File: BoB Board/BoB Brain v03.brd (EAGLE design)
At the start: 50 x 50 mm, 35 parts, among them Q1 MOSFET-NCHANNELAO3404A, Q9 MOSFET-NCHANNELAO3404A, U1 ATMEGA328P_TQFP, U3 +12v, U4 V_REG_317SMD, Y1 16MHZ

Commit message: Working on BoB board
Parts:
- removed JP2, JP3, JP4: (no value), SparkFun-Connectors:1X12
- added J1, J2, J4: (no value), SparkFun-Connectors:1X18
- moved Q9 58.0 mm to (1.80, 18.4)
- moved R17 58.0 mm to (10.9, 30.1)
- moved R19 58.0 mm to (5.90, 13.9)
- moved U4 58.0 mm to (10.1, 24.6)
- moved C10 58.0 mm to (10.8, 18.0)
- moved C11 58.0 mm to (15.0, 29.8)
- moved Q1 58.0 mm to (5.70, 18.1)
- moved R18 58.0 mm to (7.50, 32.7)
- moved R20 58.0 mm to (9.20, 14.9)
- moved R21 58.0 mm to (2.00, 21.3)
- moved R22 58.0 mm to (3.20, 23.4)
- moved U$1 56.5 mm to (18.7, 34.6), flipped to the bottom, turned to 270 degrees
- moved R11 53.1 mm to (23.1, 5.80)
- moved R12 53.0 mm to (26.6, 5.80)
- moved R13 53.0 mm to (24.9, 5.80)
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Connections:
- net N$5 renamed ATMEGA-RESET
- removed net 10: U1.14
- removed net 11: U1.15
- removed net 5: U1.9
- removed net 9: U1.13
- removed net N$10: JP4.11
- removed net N$16: JP4.10
- removed net N$17: JP4.9
- removed net N$18: JP4.8
- removed net N$19: JP4.7
- removed net N$20: JP4.6
- removed net N$21: JP4.5
- removed net N$22: JP4.4
- removed net N$23: JP4.3
- removed net N$24: JP4.2
- removed net N$25: JP4.1
- removed net N$3: U1.16
- removed net N$4: C5.2, R14.1, R2.2, S1.3, S1.4, U1.29
- removed net N$7: JP4.12
- new net 10~: J2.2, U1.14
- new net 11~: J2.1, U1.15
- new net 12: J2.6, U1.16
- new net 3~: J2.11, U1.1
- new net 4: J2.10, U1.2
- new net 5~: J2.9, U1.9
- new net 6~: J2.4, U1.10
- new net 7: J2.8, U1.11
- new net 8: J2.7, U1.12
- new net 9~: J2.3, U1.13
- new net A0: J2.18, U1.23
- new net A3: J2.15, U1.26
- new net A4-SDA: J2.14, U1.27
- new net A5-SCL: J2.13, U1.28
- new net ADC6: J2.12, U1.19
- new net ADC7: U1.22
- net 13: now also J2.5
- net 6V: now also J4.10, J4.11, J4.12, J4.13, J4.14, J4.15, J4.16, J4.17, J4.18, J4.5, J4.6, J4.7, J4.8, J4.9; no longer JP3.10, JP3.11, JP3.12, JP3.9
- net A1: now also J2.17
- net A2: now also J2.16
- net GND: now also J1.1, J1.10, J1.11, J1.12, J1.13, J1.14, J1.15, J1.16, J1.17, J1.18, J1.2, J1.3, J1.4, J1.5, J1.6, J1.7, J1.8, J1.9; no longer JP2.1, JP2.10, JP2.11, JP2.12, JP2.2, JP2.3, JP2.4, JP2.5, JP2.6, JP2.7, JP2.8, JP2.9
- net PIN_PWR: now also J4.1, J4.2, J4.3, J4.4; no longer JP3.1, JP3.2, JP3.3, JP3.4, JP3.5, JP3.6, JP3.7, JP3.8
- net RESET: now also C5.2, R14.1, R2.2, S1.3, S1.4, U1.29
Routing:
- net PIN_PWR: track 85.4 -> 0.00 mm
- net VCC: track 68.8 -> 43.1 mm
- net 6V: track 15.8 -> 0.00 mm
- net RAW: track 80.7 -> 68.7 mm
- net N$4: track 11.3 -> 0.00 mm
- net RESET: track 0.00 -> 11.2 mm
- net N$2: track 4.08 -> 0.00 mm
- net N$1: track 3.26 -> 0.00 mm
- net N$11: track 2.01 -> 0.00 mm
- net GND: vias 3 -> 2

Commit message: Routing BoB board
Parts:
- removed C4: 0.1uF, resistor:C0805K
- removed Q9: MOSFET-NCHANNELAO3404A, SparkFun-DiscreteSemi:SOT23-3
- removed R19, R21: 10k, resistor:R0805W
- added R3: 20k, resistor:R0805W
- added R4: 10k, resistor:R0805W
- R11, R12, R13: value 100k -> 470
- moved R22 35.2 mm to (38.4, 25.1), turned to 270 degrees
- moved S1 34.5 mm to (38.8, 4.10), turned to 0 degrees
- moved Q1 30.3 mm to (35.3, 24.8), turned to 0 degrees
- moved R20 27.1 mm to (33.3, 27.2), turned to 90 degrees
- moved C5 23.7 mm to (33.4, 2.90), turned to 90 degrees
- moved R2 22.1 mm to (31.0, 2.60), turned to 90 degrees
- moved C11 21.9 mm to (13.6, 7.90)
- moved R14 21.1 mm to (31.8, 6.00), turned to 180 degrees
- moved R18 18.8 mm to (4.40, 14.2), turned to 180 degrees
- moved U4 16.1 mm to (6.40, 8.90), turned to 270 degrees
- moved R17 16.0 mm to (9.10, 14.2)
- moved R1 15.9 mm to (33.5, 24.8), turned to 315 degrees
- moved C10 15.7 mm to (7.90, 2.60), turned to 180 degrees
- moved C3 8.96 mm to (20.0, 21.0)
- moved C8 8.93 mm to (18.7, 22.2), turned to 225 degrees
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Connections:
- net N$1 renamed AREF
- removed net N$12: Q1.2, R22.1, U$1.2
- removed net N$15: Q9.2, R21.1, U$1.4
- removed net N$9: LED1.5, R13.2
- new net CONN_LED: LED1.2, U$1.15
- new net N$1: LED1.5, R13.1
- new net U1_RX: Q1.3, R20.1, U1.31
- new net U1_TX: R4.2, U1.30
- new net U2-RESET: R1.2, U$1.11
- net 13: no longer LED1.2
- net 3.35V: now also LED1.1, LED1.3; no longer Q9.1, R21.2
- net 3~: now also J2.18; no longer J2.11
- net 4: now also J2.17; no longer J2.10
- net A0: now also J2.12; no longer J2.18
- net A1: now also J2.10; no longer J2.17, LED1.1, U1.24
- net A2: no longer LED1.3, U1.25
- net ADC6: now also J2.11; no longer J2.12
- net GND: now also R13.2, R3.2; no longer C4.2, R11.1, R12.1, R13.1
- net RESET: no longer R1.2, U$1.11
- net U2_RX: now also R12.1, R3.1, R4.1, U$1.4; no longer Q1.3, R20.1, U1.31
- net U2_TX: now also Q1.2, R11.1, R22.1, U$1.2; no longer Q9.3, R19.1, U1.30
- net VCC: no longer C4.1, R19.2
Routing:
- net VCC: track 43.1 -> 126.0 mm, vias 1 -> 3
- net U2_TX: track 0.00 -> 46.8 mm, vias 0 -> 2
- net 3.35V: track 0.00 -> 44.1 mm, vias 0 -> 1
- net 6V: track 0.00 -> 43.5 mm
- net RAW: track 68.7 -> 107.4 mm, vias 0 -> 2
- net 11~: track 0.00 -> 29.7 mm
- net U2-RESET: track 0.00 -> 26.3 mm, vias 0 -> 1
- net 10~: track 0.00 -> 25.9 mm
- net A0: track 0.00 -> 24.6 mm, vias 0 -> 2
- net 9~: track 0.00 -> 24.1 mm
- net U2_RX: track 0.00 -> 24.1 mm
- net 3~: track 0.00 -> 23.1 mm
- net 6~: track 0.00 -> 23.0 mm, vias 0 -> 1
- net ADC6: track 0.00 -> 22.6 mm, vias 0 -> 2
- net A1: track 0.00 -> 21.1 mm, vias 0 -> 2
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
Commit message: Working on BoB Board
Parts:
- moved R2 25.2 mm to (12.3, 19.5)
- moved R11 11.3 mm to (19.0, 16.3), turned to 0 degrees
- moved R13 10.5 mm to (19.0, 14.5), turned to 180 degrees
- moved R12 10.3 mm to (19.0, 12.8), turned to 0 degrees
- moved R4 8.21 mm to (20.9, 20.0), turned to 270 degrees
- moved R3 3.45 mm to (17.9, 21.1), turned to 0 degrees
- moved LED1 2.80 mm to (24.9, 14.5), turned to 180 degrees
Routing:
- net 3.35V: track 44.1 -> 64.0 mm
- net U1_TX: track 3.62 -> 17.2 mm
- net U2_TX: track 46.8 -> 58.1 mm
- net U2_RX: track 24.1 -> 31.4 mm, vias 0 -> 1
- net N$3: track 0.00 -> 2.49 mm
- net N$4: track 0.00 -> 2.45 mm
- net N$1: track 0.00 -> 2.45 mm
- net VCC: track 126.0 -> 124.1 mm
- net A1: track 21.1 -> 19.3 mm
- net U2-RESET: track 26.3 -> 27.2 mm

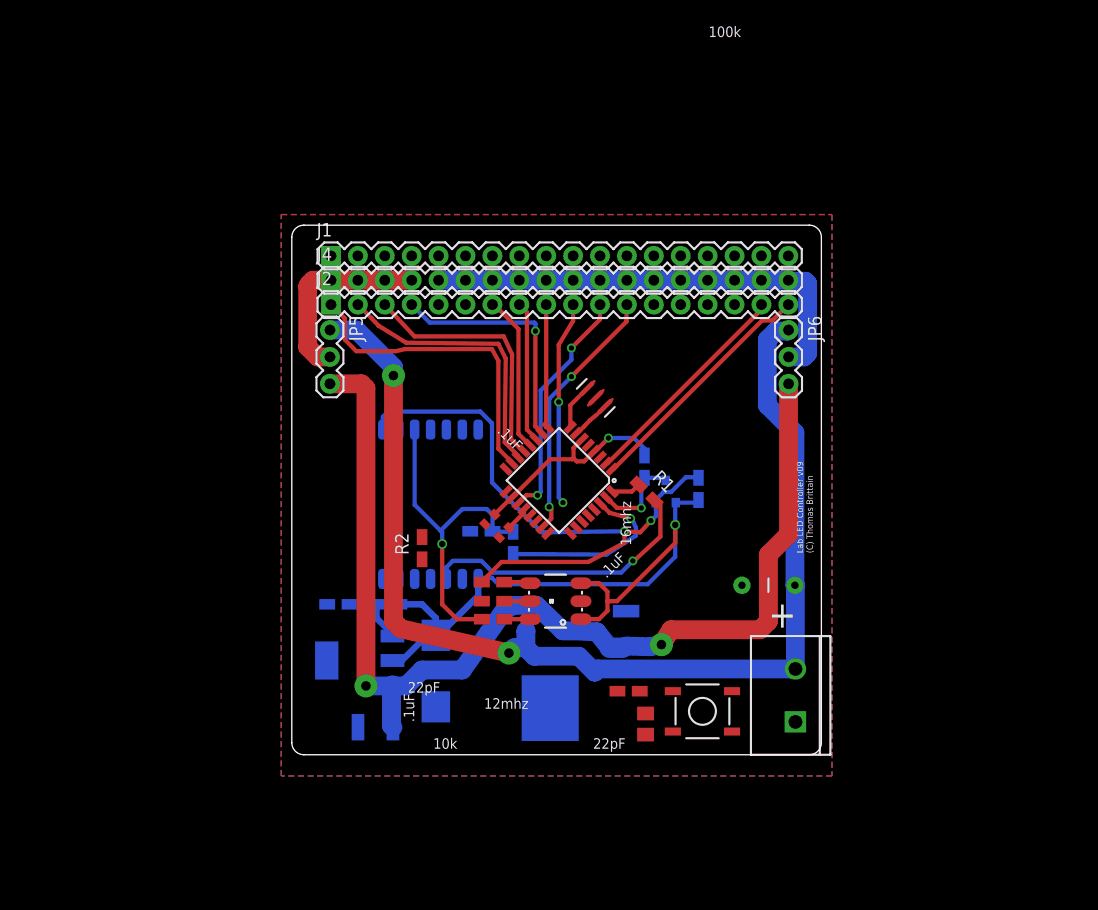
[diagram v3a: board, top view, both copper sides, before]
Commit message: Finished routing BoB Board
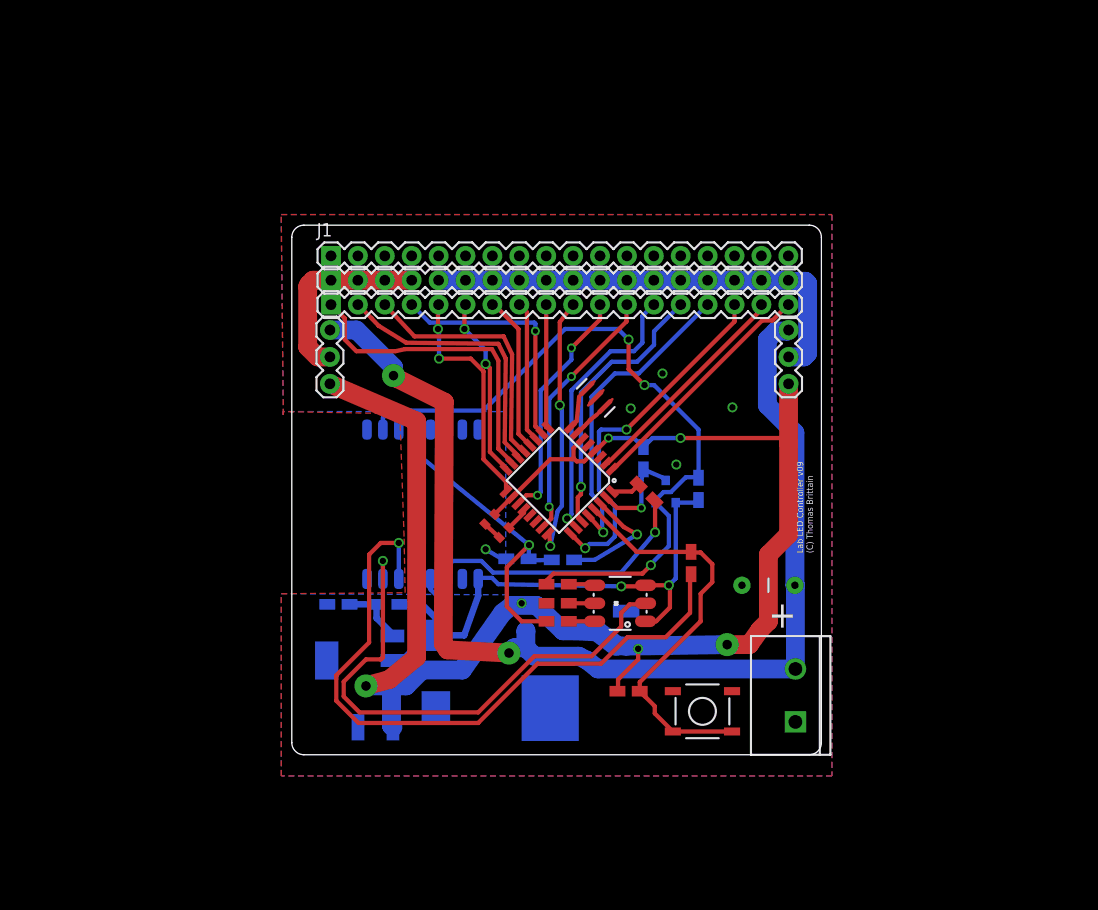
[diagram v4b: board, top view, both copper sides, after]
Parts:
- removed C5: 0.1uF, resistor:C0805K
- moved R2 25.4 mm to (37.7, 18.1)
- moved LED1 6.10 mm to (31.0, 14.3)
- moved R11 6.10 mm to (25.1, 16.1)
- moved R12 6.10 mm to (25.1, 12.6)
- moved R13 6.10 mm to (25.1, 14.3)
- moved R4 4.96 mm to (25.6, 18.4), turned to 180 degrees
- moved R3 4.28 mm to (21.3, 18.5)
- moved R20 0.81 mm to (33.2, 28.0)
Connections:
- removed net DTR: C5.1
- net A1: now also U1.24
- net A2: now also U1.25
- net A3: now also J2.13; no longer J2.15
- net A5-SCL: now also J2.15; no longer J2.13
- net RESET: no longer C5.2
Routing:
- net ATMEGA-RESET: track 0.00 -> 64.0 mm, vias 0 -> 1
- net CONN_LED: track 0.00 -> 51.0 mm, vias 0 -> 1
- net RESET: track 0.00 -> 39.6 mm
- net A2: track 0.00 -> 34.5 mm, vias 0 -> 2
- net A5-SCL: track 0.00 -> 29.9 mm, vias 0 -> 1
- net A3: track 0.00 -> 26.5 mm, vias 0 -> 1
- net A4-SDA: track 0.00 -> 26.1 mm, vias 0 -> 1
- net VCC: track 124.1 -> 149.8 mm, vias 3 -> 5
- net 13: track 0.00 -> 22.1 mm, vias 0 -> 2
- net 12: track 0.00 -> 17.2 mm, vias 0 -> 2
- net 3.35V: track 64.0 -> 53.5 mm, vias 1 -> 2
- net U2_TX: track 58.1 -> 67.6 mm, vias 2 -> 3
- net GND: track 0.00 -> 6.89 mm, vias 0 -> 6
- net U1_TX: track 17.2 -> 11.2 mm
- net A1: track 19.3 -> 24.8 mm
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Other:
- board text removed: ".1uF"
- board text removed: "100k"
- board text removed: "10k"
- board text removed: "10uF"
- board text removed: "12mhz"
- board text removed: "16mhz"
- board text removed: "20k"
- board text removed: "22pF"
